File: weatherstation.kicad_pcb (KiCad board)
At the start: 2 copper layers, 1 part, among them U1 ESP-12E

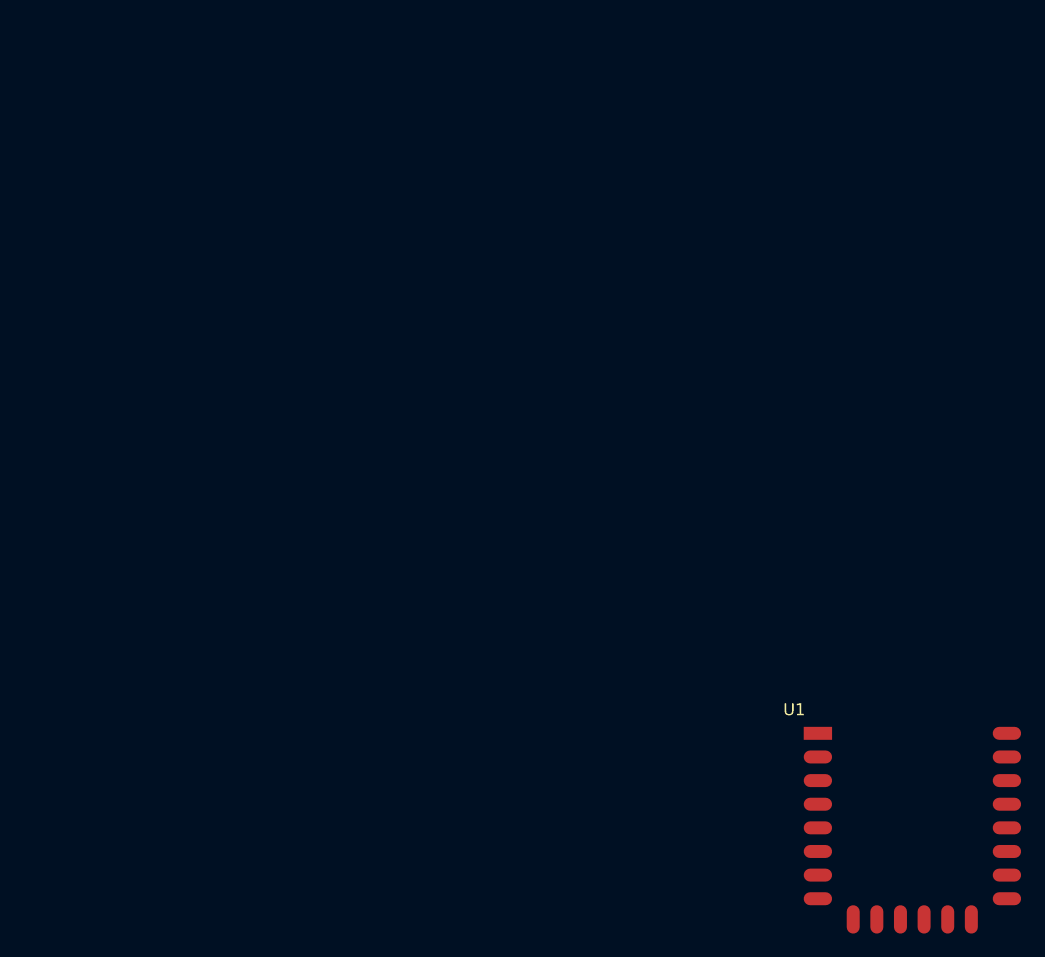
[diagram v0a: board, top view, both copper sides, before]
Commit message: Added a USB socket with GND set as a power output to pass DRC, and gave a first stab at a placement. Man that's tight! Components both side required??
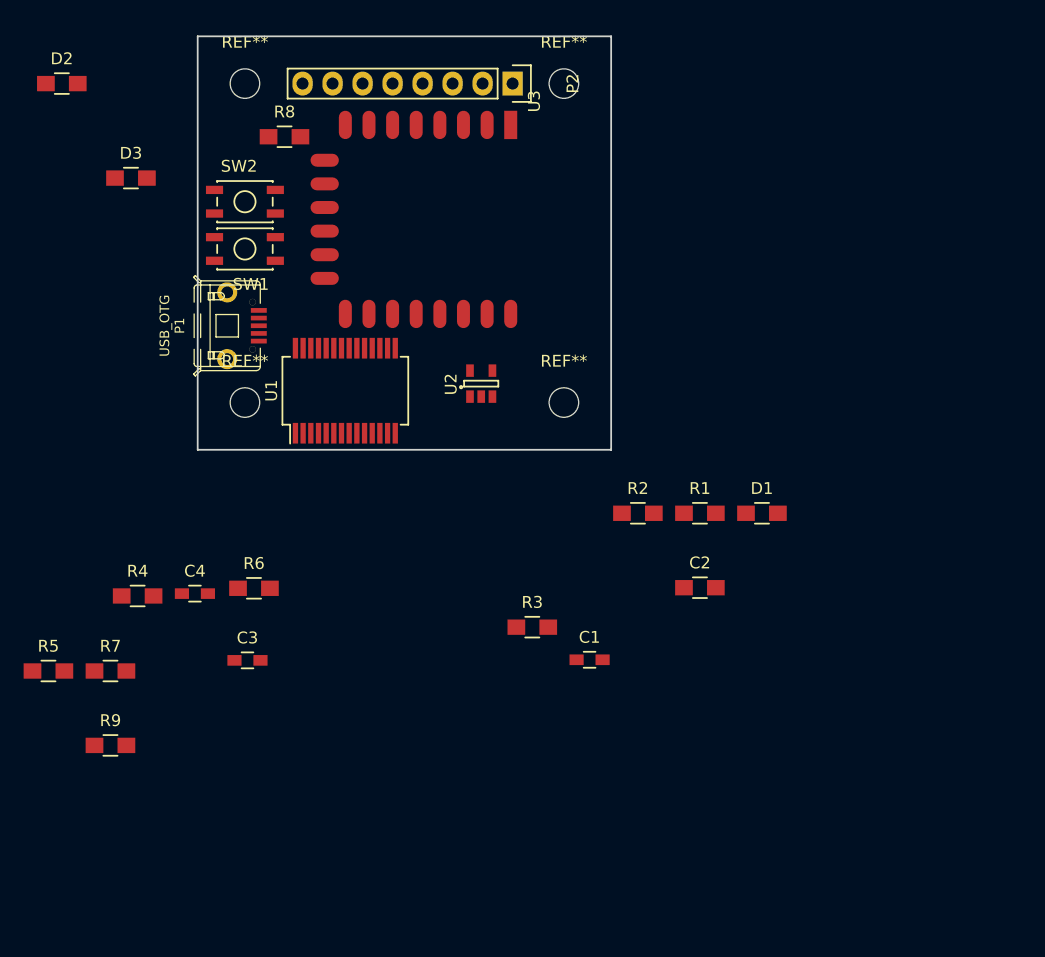
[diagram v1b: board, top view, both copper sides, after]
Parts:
- added C1: 100n, Resistors_SMD:R_0603_HandSoldering, F.Cu at (129.2, 98.8)
- added C2: 10u, Resistors_SMD:R_0805_HandSoldering, F.Cu at (138.5, 92.7)
- added C3: 10u, Resistors_SMD:R_0603_HandSoldering, F.Cu at (100.2, 98.8)
- added C4: 10u, Resistors_SMD:R_0603_HandSoldering, F.Cu at (95.8, 93.2)
- added D1: LED, Resistors_SMD:R_0805_HandSoldering, F.Cu at (143.8, 86.4)
- added D2: LED, Resistors_SMD:R_0805_HandSoldering, F.Cu at (84.5, 50.0)
- added D3: LED, Resistors_SMD:R_0805_HandSoldering, F.Cu at (90.3, 58.0)
- added P1: USB_OTG, ab2_usb:AB2_USB_MICRO_SMD, F.Cu at (95.8, 70.5)
- added P2: CONN_01X08, Pin_Headers:Pin_Header_Straight_1x08, F.Cu at (122.7, 50.0)
- added R1: 10R, Resistors_SMD:R_0805_HandSoldering, F.Cu at (138.5, 86.4)
- added R2: 1k, Resistors_SMD:R_0805_HandSoldering, F.Cu at (133.3, 86.4)
- added R3: 1k, Resistors_SMD:R_0805_HandSoldering, F.Cu at (124.3, 96.0)
- added R4: 10k, Resistors_SMD:R_0805_HandSoldering, F.Cu at (90.9, 93.4)
- added R5: 10k, Resistors_SMD:R_0805_HandSoldering, F.Cu at (83.4, 99.7)
- added R6: 10k, Resistors_SMD:R_0805_HandSoldering, F.Cu at (100.8, 92.7)
- added R7: 10k, Resistors_SMD:R_0805_HandSoldering, F.Cu at (88.6, 99.7)
- added R8: 10k, Resistors_SMD:R_0805_HandSoldering, F.Cu at (103.3, 54.5)
- added R9: 10k, Resistors_SMD:R_0805_HandSoldering, F.Cu at (88.6, 106.0)
- added REF**: MountingHole_2-5mm, Mounting_Holes:MountingHole_2-5mm, F.Cu at (100.0, 50.0)
- added REF**: MountingHole_2-5mm, Mounting_Holes:MountingHole_2-5mm, F.Cu at (127.0, 50.0)
- added REF**: MountingHole_2-5mm, Mounting_Holes:MountingHole_2-5mm, F.Cu at (100.0, 77.0)
- added REF**: MountingHole_2-5mm, Mounting_Holes:MountingHole_2-5mm, F.Cu at (127.0, 77.0)
- added SW1: SW_PUSH, Buttons_Switches_SMD:SW_SPST_EVQP2, F.Cu at (100.0, 64.0)
- added SW2: SW_PUSH, Buttons_Switches_SMD:SW_SPST_EVQP2, F.Cu at (100.0, 60.0)
- added U2: APE8865Y5-33-HF-3, Housings_SOT-23_SOT-143_TSOT-6:SOT-23-5, F.Cu at (120.0, 75.4)
- added U3: ESP-12E, ESP8266:ESP-12E, F.Cu at (122.5, 53.5)
- U1: value ESP-12E -> FT232RL; footprint ESP8266:ESP-12E -> Housings_SSOP:SSOP-28_5.3x10.2mm_Pitch0.65mm
- moved U1 49.4 mm to (108.5, 76.0), turned to 90 degrees
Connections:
- U1 pad 18: Net-(U1-Pad18) -> GNDPWR
- U1 pad 20: Net-(U1-Pad20) -> +5V
- U1 pad 21: Net-(U1-Pad21) -> GNDPWR
- U1 pad 4: Net-(U1-Pad4) -> Net-(U1-Pad17)
- U1 pad 5: Net-(U1-Pad5) -> /ESP_module/ESP_OUT_TXD
- U1 pad 7: Net-(U1-Pad7) -> GNDPWR
- U1 pad 8: Net-(U1-Pad8) -> (no net)
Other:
- board outline added: 35 x 35 mm

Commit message: Dodgy layout added, etc
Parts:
- P1: footprint ab2_usb:AB2_USB_MICRO_SMD -> usb:USB_Micro-B
- SW1, SW2: footprint Buttons_Switches_SMD:SW_SPST_EVQP2 -> EVQP2:SW_SPST_EVQP2
- moved R5 60.7 mm to (122.2, 53.0)
- moved C1 51.4 mm to (106.9, 52.5), turned to 180 degrees
- moved D1 47.5 mm to (117.2, 47.0), turned to 180 degrees
- moved R3 43.7 mm to (116.7, 53.0)
- moved C3 43.2 mm to (106.5, 56.1), turned to 270 degrees
- moved R9 42.6 mm to (107.8, 68.0), turned to 180 degrees
- moved R2 40.7 mm to (122.8, 47.0), turned to 180 degrees
- moved C2 37.6 mm to (104.0, 77.8), turned to 90 degrees
- moved C4 34.9 mm to (109.5, 61.1), turned to 270 degrees
- moved R7 34.3 mm to (110.0, 72.8), turned to 270 degrees
- moved R1 33.9 mm to (107.5, 72.7), turned to 270 degrees
- moved R4 33.0 mm to (107.8, 65.0)
- moved SW1 24.7 mm to (120.0, 78.5)
- moved D3 24.0 mm to (111.7, 47.0), turned to 180 degrees
- moved R8 23.6 mm to (106.5, 77.8), turned to 270 degrees
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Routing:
- net GNDPWR: track 0.00 -> 114.3 mm, vias 0 -> 7
- net +5V: track 0.00 -> 94.9 mm, vias 0 -> 5
- net +3.3VP: track 0.00 -> 59.3 mm, vias 0 -> 6
- net /ESP_module/ESP_RESET: track 0.00 -> 55.8 mm, vias 0 -> 2
- net /display/DISP_RST: track 0.00 -> 42.8 mm, vias 0 -> 5
- net /ESP_module/ESP_GPIO0: track 0.00 -> 36.8 mm, vias 0 -> 3
- net /ESP_module/ESP_CH_PD: track 0.00 -> 29.9 mm, vias 0 -> 2
- net /ESP_module/ESP_OUT_TXD: track 0.00 -> 29.9 mm
- net Net-(D1-Pad2): track 0.00 -> 28.7 mm, vias 0 -> 2
- net /ESP_module/ESP_IN_RXD: track 0.00 -> 25.2 mm
- net /display/DISP_SDA: track 0.00 -> 21.2 mm, vias 0 -> 3
- net /ESP_module/ESP_GPIO15: track 0.00 -> 20.0 mm
- net Net-(P1-Pad3): track 0.00 -> 18.9 mm
- net Net-(U1-Pad17): track 0.00 -> 18.0 mm
- net Net-(D2-Pad1): track 0.00 -> 17.9 mm
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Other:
- net class Default: via_dia 0.6 -> 0.7; via_drill 0.4 -> 0.5
- net class Large added: clearance 0.4, trace_width 0.5, via_dia 0.7, via_drill 0.5
- rule via_min_drill: 0.3 -> 0.5
- rule via_min_size: 0.4 -> 0.7

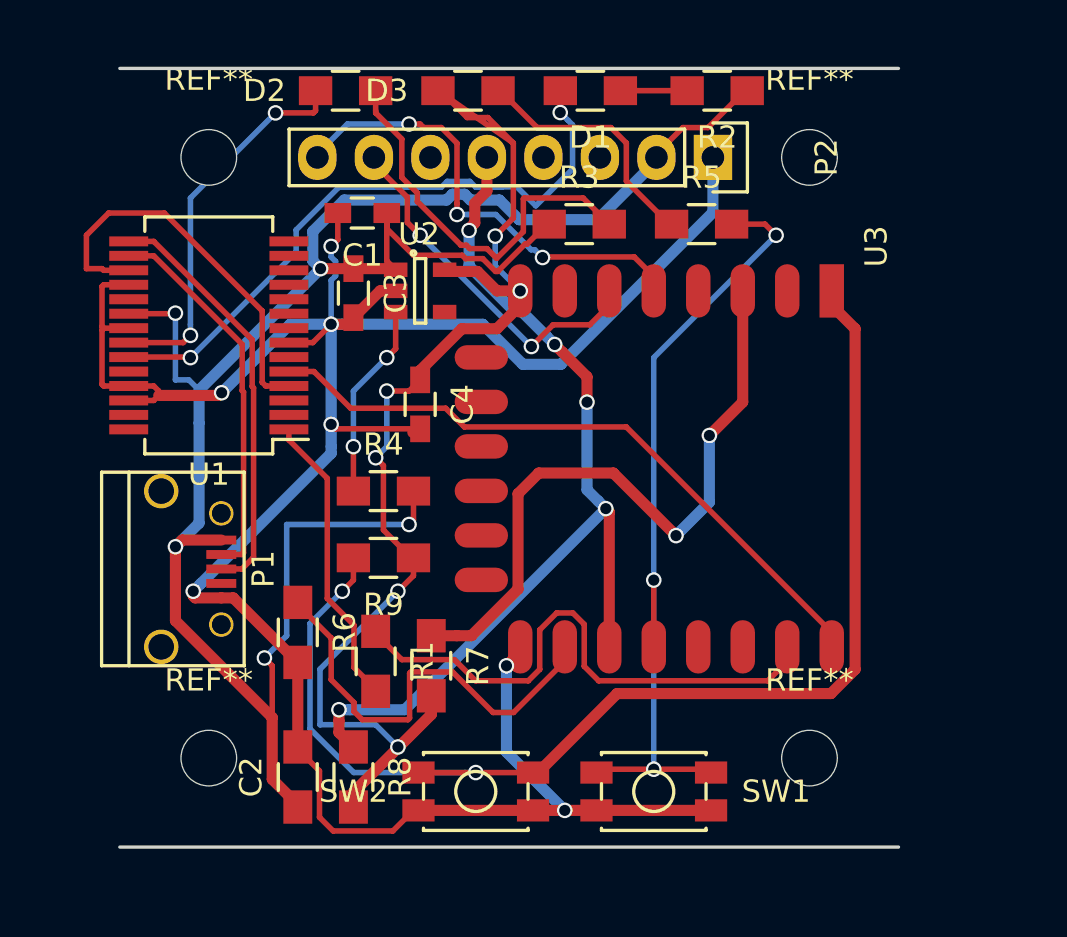
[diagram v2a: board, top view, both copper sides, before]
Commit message: Fixed layout up a bit
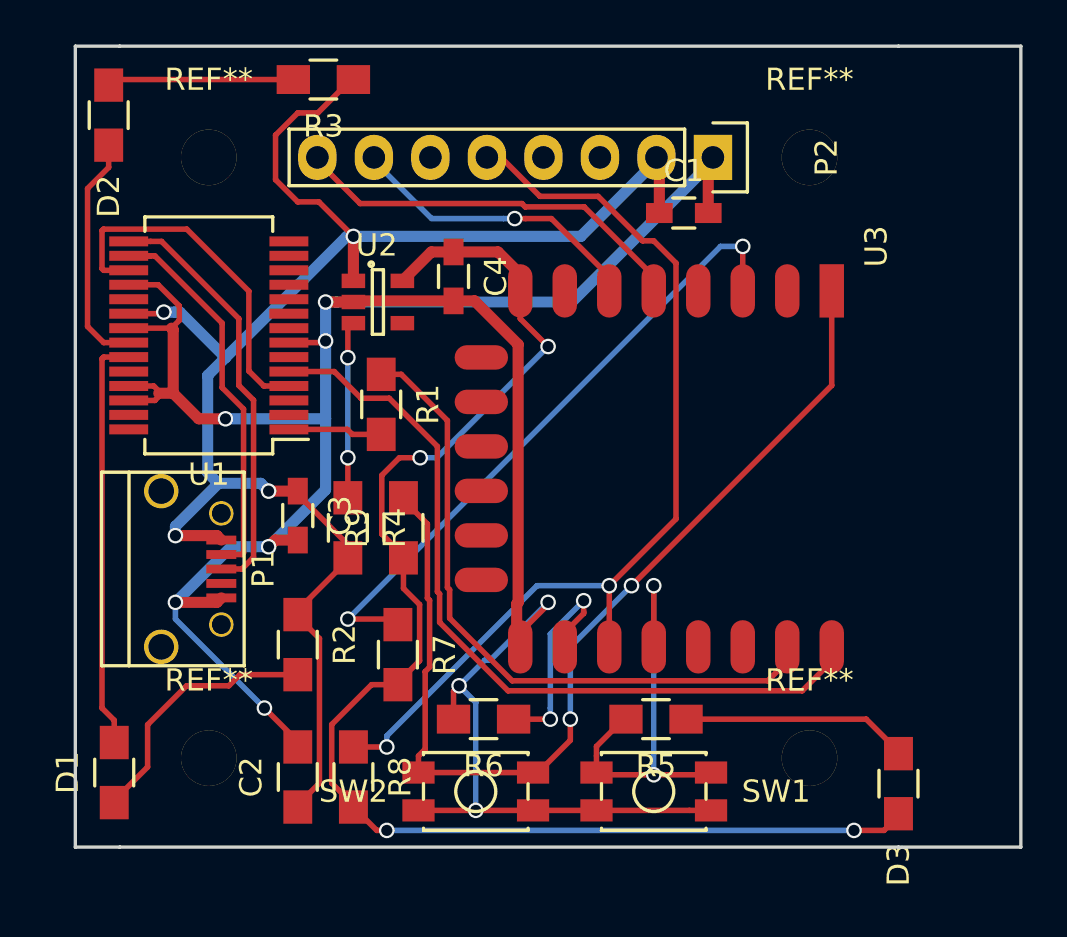
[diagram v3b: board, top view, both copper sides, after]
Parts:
- moved D1 37.4 mm to (95.8, 77.7), turned to 90 degrees
- moved D3 36.7 mm to (131.0, 78.2), turned to 270 degrees
- moved R2 31.2 mm to (104.0, 71.9), turned to 270 degrees
- moved R5 22.3 mm to (120.1, 75.2), turned to 180 degrees
- moved C1 14.4 mm to (121.3, 52.5), turned to 0 degrees
- moved R3 13.2 mm to (105.2, 46.5), turned to 180 degrees
- moved R1 11.6 mm to (107.8, 61.1)
- moved D2 10.7 mm to (95.5, 48.1), turned to 270 degrees
- moved C3 10.3 mm to (104.0, 66.1)
- moved R6 9.22 mm to (112.3, 75.2), turned to 180 degrees
- moved C4 5.94 mm to (111.0, 55.4)
- moved R4 2.30 mm to (106.2, 66.7), turned to 270 degrees
- moved U2 1.96 mm to (107.6, 56.5)
- moved R9 1.62 mm to (108.8, 66.7), turned to 90 degrees
- moved R7 1.58 mm to (108.5, 72.3)
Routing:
- net +5V: track 94.9 -> 76.7 mm, vias 5 -> 4
- net /ESP_module/ESP_GPIO0: track 36.8 -> 19.7 mm, vias 3 -> 2
- net GNDPWR: track 114.3 -> 126.4 mm, vias 7 -> 9
- net /ESP_module/ESP_RESET: track 55.8 -> 45.5 mm
- net Net-(D1-Pad2): track 28.7 -> 18.7 mm, vias 2 -> 0
- net /ESP_module/ESP_GPIO15: track 20.0 -> 10.0 mm, vias 0 -> 2
- net Net-(D2-Pad1): track 17.9 -> 8.40 mm
- net Net-(R1-Pad2): track 13.4 -> 4.24 mm
- net Net-(D1-Pad1): track 3.00 -> 11.8 mm
- net Net-(D2-Pad2): track 17.2 -> 10.7 mm, vias 2 -> 0
- net /ESP_module/ESP_OUT_TXD: track 29.9 -> 36.1 mm
- net /ESP_module/ESP_IN_RXD: track 25.2 -> 30.1 mm
- net +3.3VP: track 59.3 -> 63.8 mm, vias 6 -> 4
- net /display/DISP_SDA: track 21.2 -> 18.1 mm, vias 3 -> 0
- net /display/DISP_SCL: track 16.3 -> 13.5 mm, vias 2 -> 1
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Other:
- board size 35 x 35 mm -> 42.5 x 36 mm

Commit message: Added logo, sensor, manufacturing data'
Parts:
- added G***: LOGO, ESP_WeatherStation:techcity_logo, B.Cu at (126.4, 62.6)
- added IC1: TMP100, SOT-23-6, F.Cu at (133.1, 48.1)
- added REF**: Symbol_OSHW-Logo_SilkScreen, Symbols:Symbol_OSHW-Logo_SilkScreen, B.Cu at (103.9, 63.3)
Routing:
- net /display/DISP_SDA: track 18.1 -> 46.6 mm, vias 0 -> 1
- net /display/DISP_SCL: track 13.5 -> 39.6 mm, vias 1 -> 2
- net +5V: track 76.7 -> 94.0 mm
- net GNDPWR: track 126.4 -> 142.3 mm
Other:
- board text added: "Weather Widget Gary Fletcher Ryan White"

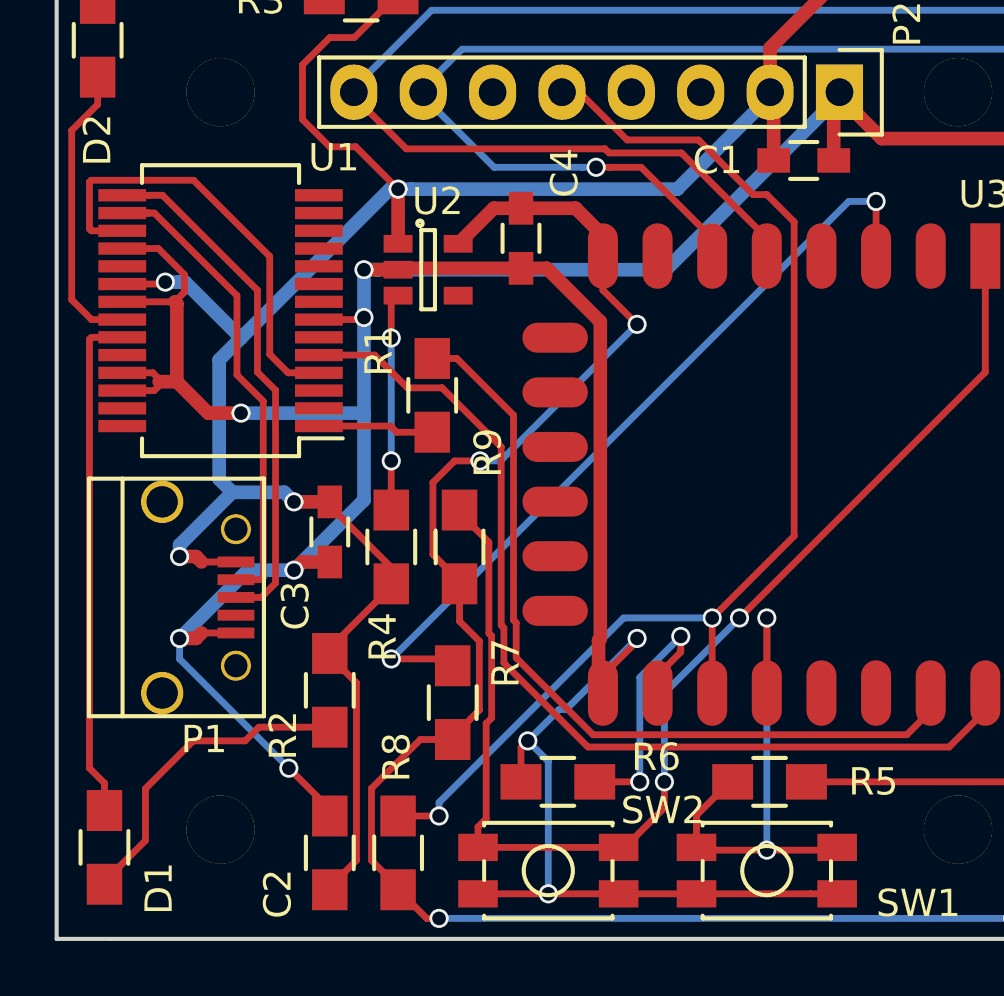
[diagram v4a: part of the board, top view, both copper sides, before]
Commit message: Added BOM with RS numbers
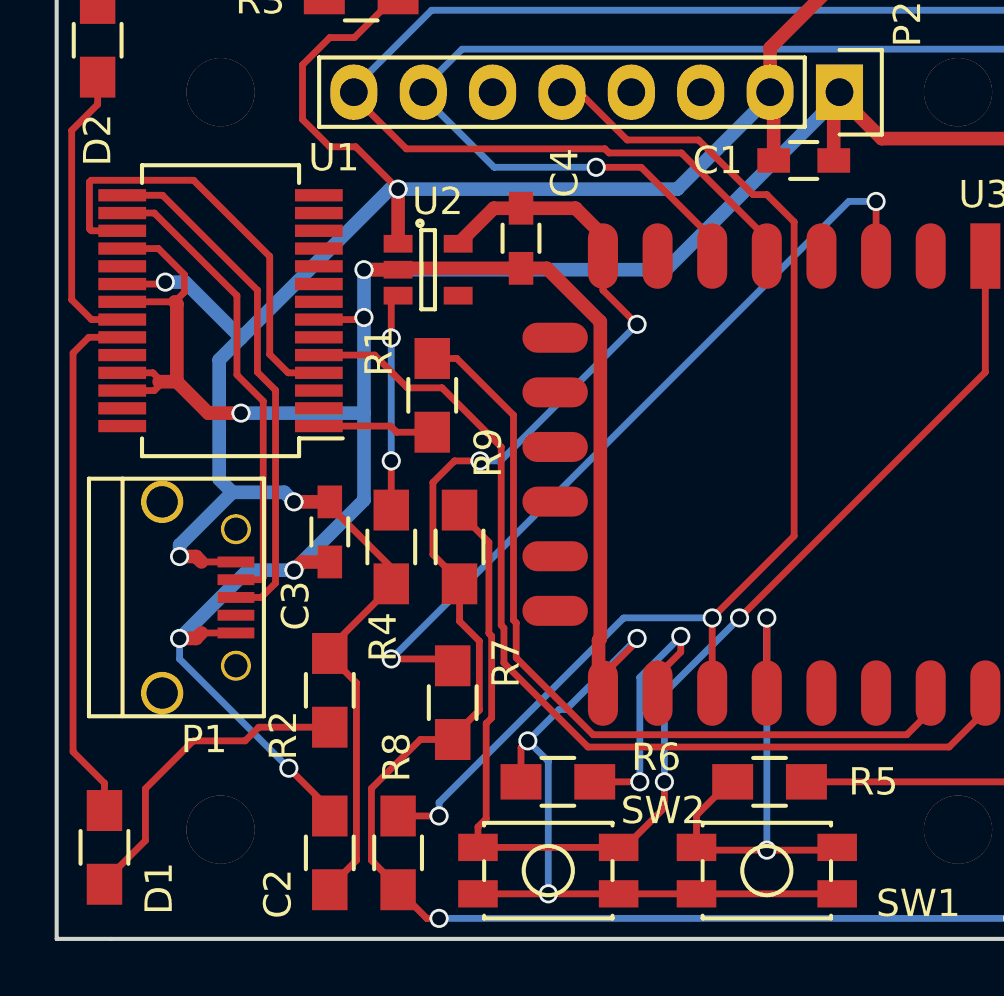
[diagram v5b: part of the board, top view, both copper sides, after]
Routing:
- net Net-(P1-Pad2): track 18.2 -> 17.2 mm
- net +5V: track 94.0 -> 93.4 mm
- net Net-(D1-Pad2): track 18.7 -> 19.3 mm

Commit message: Added manufacturing files, fixed rear text, moved tracks away from mounting holes and added vias to ground plane
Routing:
- net GNDPWR: track 142.3 -> 97.4 mm, vias 9 -> 14
- net /display/DISP_SCL: track 39.6 -> 41.0 mm
- net Net-(D3-Pad1): track 10.3 -> 11.6 mm
- added copper zone on B.Cu, net GNDPWR
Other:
- board text added: "IoT Widget Ryan White Gary Fletcher"
- board text removed: "Weather Widget Gary Fletcher Ryan White"
